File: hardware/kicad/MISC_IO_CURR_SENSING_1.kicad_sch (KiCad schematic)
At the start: 20 parts

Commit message: starting erc check
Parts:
- C39: footprint Capacitor_SMD:C_0603_1608Metric -> 5v rail sm-easyedapro:C0603
- C40: footprint Capacitor_SMD:C_0805_2012Metric -> 5v rail sm-easyedapro:C0805
- C41, C42, C43: footprint Capacitor_SMD:C_0201_0603Metric -> 5v rail sm-easyedapro:C0201
- CUR_1: footprint Package_DFN_QFN:QFN-16-1EP_4x4mm_P0.65mm_EP2.2x2.2mm -> 5v rail sm-easyedapro:QFN-16_L4.0-W4.0-P0.65-TL-EP2.2
- R100, R101, R102, R96, R97, R99: footprint Resistor_SMD:R_0402_1005Metric -> 5v rail sm-easyedapro:R0402; LCSC Part Name 10Ω ±1% 50mW 厚膜电阻 -> 厚膜电阻 10Ω ±1% 62.5mW; Manufacturer UNI-ROYAL(厚声) -> YAGEO(国巨); Manufacturer Part 0201WMF100JTEE -> RC0402FR-0710RL; Supplier Part C270817 -> C138066
- R98: footprint Resistor_SMD:R_0402_1005Metric -> 5v rail sm-easyedapro:R0402; LCSC Part Name 厚膜电阻 10kΩ ±1% 50mW -> 10kΩ ±1% 62.5mW 厚膜电阻; Manufacturer YAGEO(国巨) -> UNI-ROYAL(厚声); Manufacturer Part RC0201FR-0710KL -> 0402WGF1002TCE; Supplier Part C106225 -> C25744

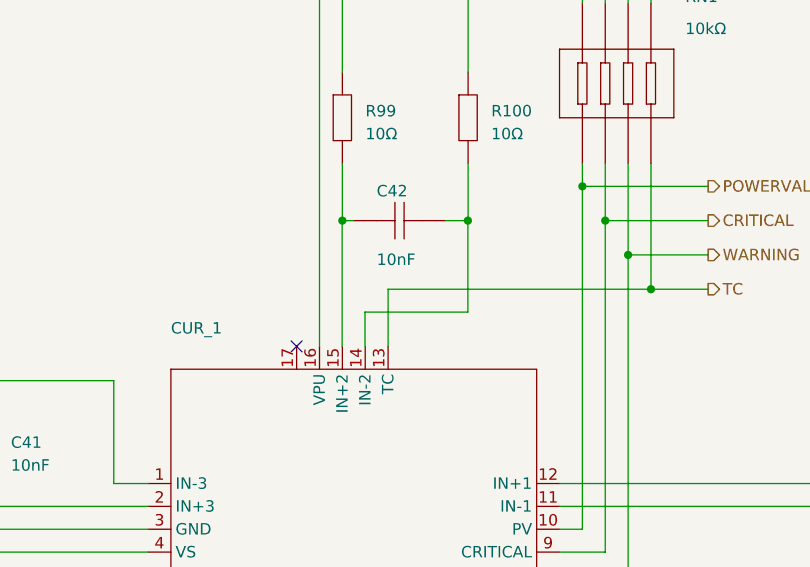
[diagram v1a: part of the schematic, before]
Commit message: current sensor done for breakout ports
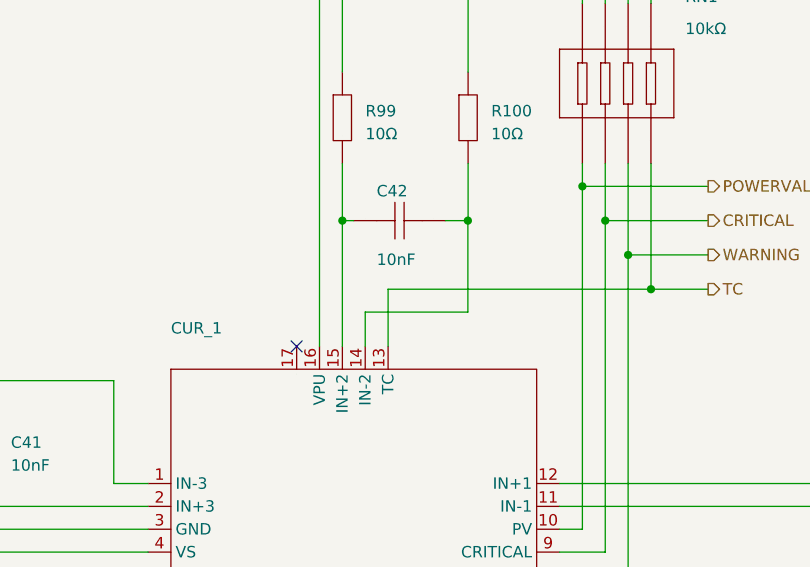
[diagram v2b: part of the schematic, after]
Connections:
- net at CUR_1.14 (IN-2): now also C42.2, R100.2
- net at CUR_1.15 (IN+2): now also C42.1, R99.2
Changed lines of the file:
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@@
 	(wire
 		(pts
-			(xy 154.9146 80.01) (xy 154.9146 93.98)
+			(xy 154.94 80.01) (xy 154.94 93.98)
 		)
 		(stroke
@@
 	(wire
 		(pts
-			(xy 157.4546 93.98) (xy 157.4546 90.17)
+			(xy 157.48 93.98) (xy 157.48 90.17)
 		)
 		(stroke
@@
 	(wire
 		(pts
-			(xy 154.94 80.01) (xy 154.9146 80.01)
-		)
-		(stroke
-			(width 0)
-			(type default)
-		)
-	)
-	(wire
-		(pts
 			(xy 181.61 73.66) (xy 181.61 76.2)
 		)
@@
 	(wire
 		(pts
-			(xy 168.8846 90.17) (xy 157.4546 90.17)
-		)
-		(stroke
+			(xy 168.8846 90.17) (xy 157.48 90.17)
+		)
+		(stroke

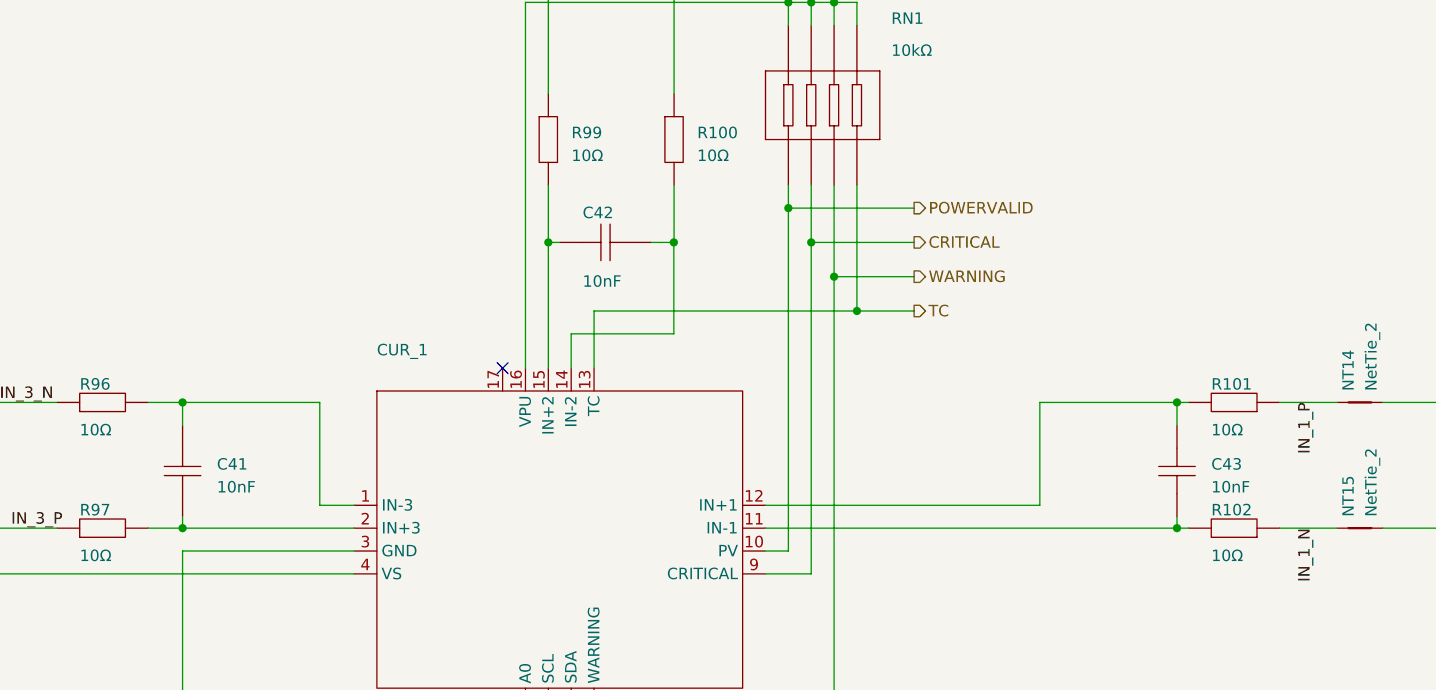
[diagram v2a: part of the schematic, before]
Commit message: flipped spots for 12v ports
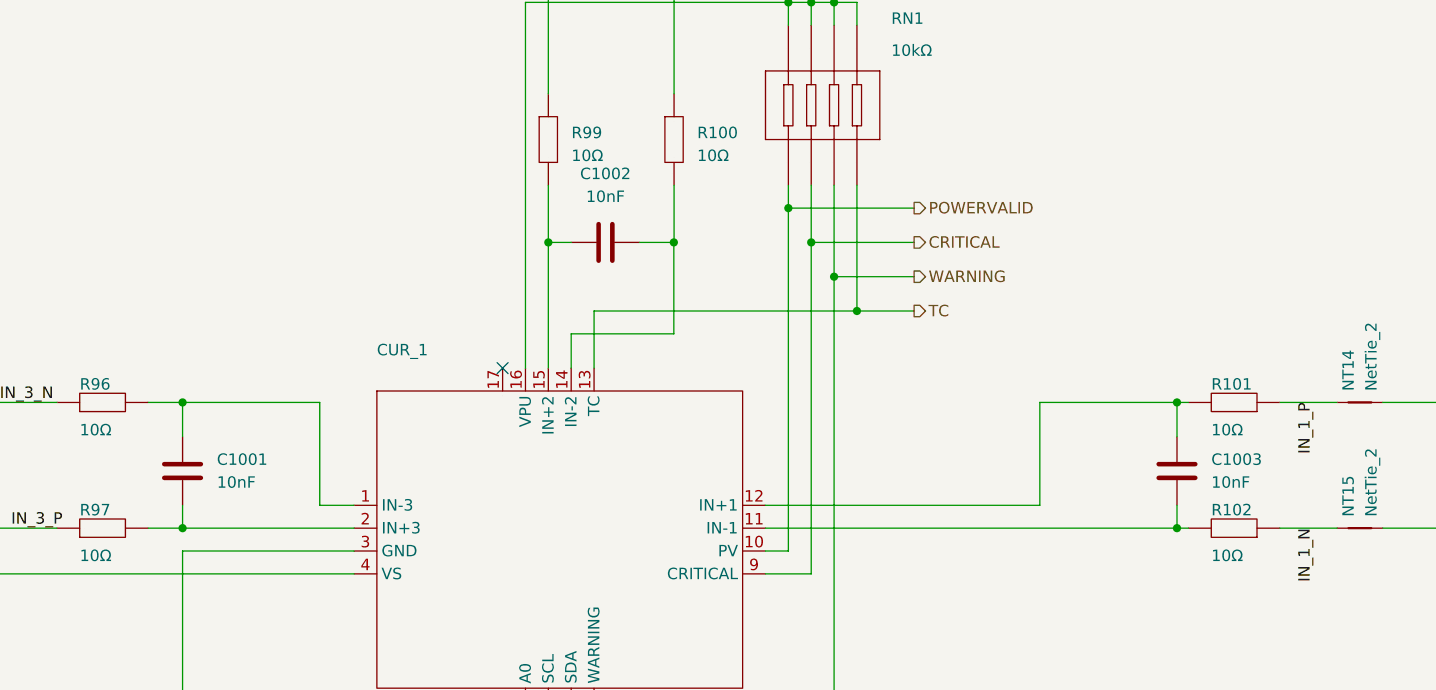
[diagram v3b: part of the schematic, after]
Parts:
- removed C41, C42, C43: 10nF, 5v rail sm-easyedapro:C0201, symbol 5v rail sm-easyedapro:TCC0201X7R103K500ZT
- added C1001, C1002, C1003: 10nF, Capacitor_SMD:C_0402_1005Metric, symbol Device:C
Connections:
- net at CUR_1.1 (IN-3), R96.2: now also C1001.1
- net at CUR_1.11 (IN-1), R102.2: now also C1003.1
- net at CUR_1.12 (IN+1), R101.2: now also C1003.2
- net at CUR_1.14 (IN-2), R100.2: now also C1002.2
- net at CUR_1.15 (IN+2), R99.2: now also C1002.1
- net at CUR_1.2 (IN+3), R97.2: now also C1001.2

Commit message: updating symbols to use kicad footprints where possible
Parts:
- C39: footprint 5v rail sm-easyedapro:C0603 -> Capacitor_SMD:C_0603_1608Metric
- C40: footprint 5v rail sm-easyedapro:C0805 -> Capacitor_SMD:C_0805_2012Metric
- R100, R101, R102, R96, R97, R98, R99: footprint 5v rail sm-easyedapro:R0402 -> Resistor_SMD:R_0402_1005Metric
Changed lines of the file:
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@@
 			)
 		)
-		(property "Footprint" "5v rail sm-easyedapro:R0402"
+		(property "Footprint" "Resistor_SMD:R_0402_1005Metric"
 			(at 231.14 111.76 0)
 			(effects
@@
 			)
 		)
-		(property "Footprint" "5v rail sm-easyedapro:R0402"
+		(property "Footprint" "Resistor_SMD:R_0402_1005Metric"
 			(at 142.24 138.43 0)
 			(effects
@@
 			)
 		)
-		(property "Footprint" "5v rail sm-easyedapro:R0402"
+		(property "Footprint" "Resistor_SMD:R_0402_1005Metric"
 			(at 168.91 68.58 0)
 			(effects
@@
 			)
 		)
-		(property "Footprint" "5v rail sm-easyedapro:C0805"
+		(property "Footprint" "Capacitor_SMD:C_0805_2012Metric"
 			(at 63.5 127 0)
 			(effects
@@
 			)
 		)
-		(property "Footprint" "5v rail sm-easyedapro:R0402"
+		(property "Footprint" "Resistor_SMD:R_0402_1005Metric"
 			(at 105.41 111.76 0)
 			(effects
@@
 			)
 		)
-		(property "Footprint" "5v rail sm-easyedapro:R0402"
+		(property "Footprint" "Resistor_SMD:R_0402_1005Metric"
 			(at 154.94 68.58 0)
 			(effects
@@
 			)
 		)
-		(property "Footprint" "5v rail sm-easyedapro:C0603"
+		(property "Footprint" "Capacitor_SMD:C_0603_1608Metric"
 			(at 46.99 127 0)
 			(effects
@@
 			)
 		)
-		(property "Footprint" "5v rail sm-easyedapro:R0402"
+		(property "Footprint" "Resistor_SMD:R_0402_1005Metric"
 			(at 231.14 97.79 0)
 			(effects
@@
 			)
 		)
-		(property "Footprint" "5v rail sm-easyedapro:R0402"
+		(property "Footprint" "Resistor_SMD:R_0402_1005Metric"
 			(at 105.41 97.79 0)
 			(effects

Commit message: switched some more
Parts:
- CUR_1: footprint 5v rail sm-easyedapro:QFN-16_L4.0-W4.0-P0.65-TL-EP2.2 -> Package_DFN_QFN:QFN-16-1EP_4x4mm_P0.65mm_EP2.2x2.2mm
- RN1: footprint 5v rail sm-easyedapro:RES-ARRAY-SMD_0603-8P-L3.2-W1.6-BL -> Resistor_SMD:R_Array_Convex_4x0603
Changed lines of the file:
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@@
 			)
 		)
-		(property "Footprint" "5v rail sm-easyedapro:QFN-16_L4.0-W4.0-P0.65-TL-EP2.2"
+		(property "Footprint" "Package_DFN_QFN:QFN-16-1EP_4x4mm_P0.65mm_EP2.2x2.2mm"
 			(at 156.21 113.03 0)
 			(effects
@@
 			)
 		)
-		(property "Footprint" "5v rail sm-easyedapro:RES-ARRAY-SMD_0603-8P-L3.2-W1.6-BL"
+		(property "Footprint" "Resistor_SMD:R_Array_Convex_4x0603"
 			(at 185.42 64.77 0)
 			(effects

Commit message: various erc fixes
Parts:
- CUR_1: footprint Package_DFN_QFN:QFN-16-1EP_4x4mm_P0.65mm_EP2.2x2.2mm -> Package_DFN_QFN:Texas_RGV0016A_VQFN-16-1EP_4x4mm_P0.65mm_EP2.1x2.1mm
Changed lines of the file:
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@@
 			)
 		)
-		(property "Footprint" "Package_DFN_QFN:QFN-16-1EP_4x4mm_P0.65mm_EP2.2x2.2mm"
+		(property "Footprint" "Package_DFN_QFN:Texas_RGV0016A_VQFN-16-1EP_4x4mm_P0.65mm_EP2.1x2.1mm"
 			(at 156.21 113.03 0)
 			(effects

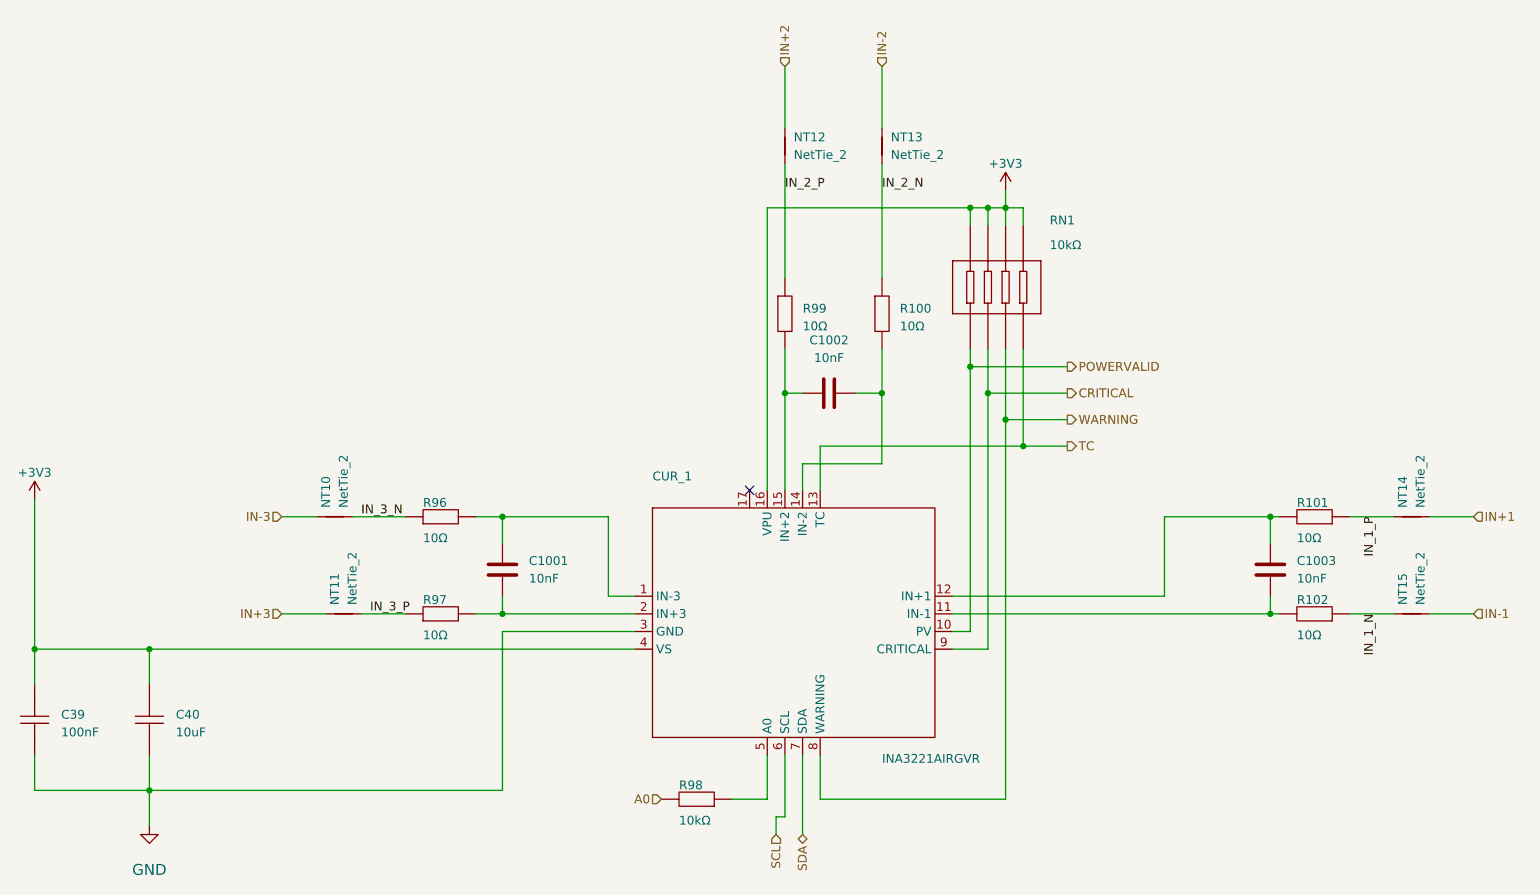
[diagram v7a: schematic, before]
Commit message: fixing inconsistencies in value convention
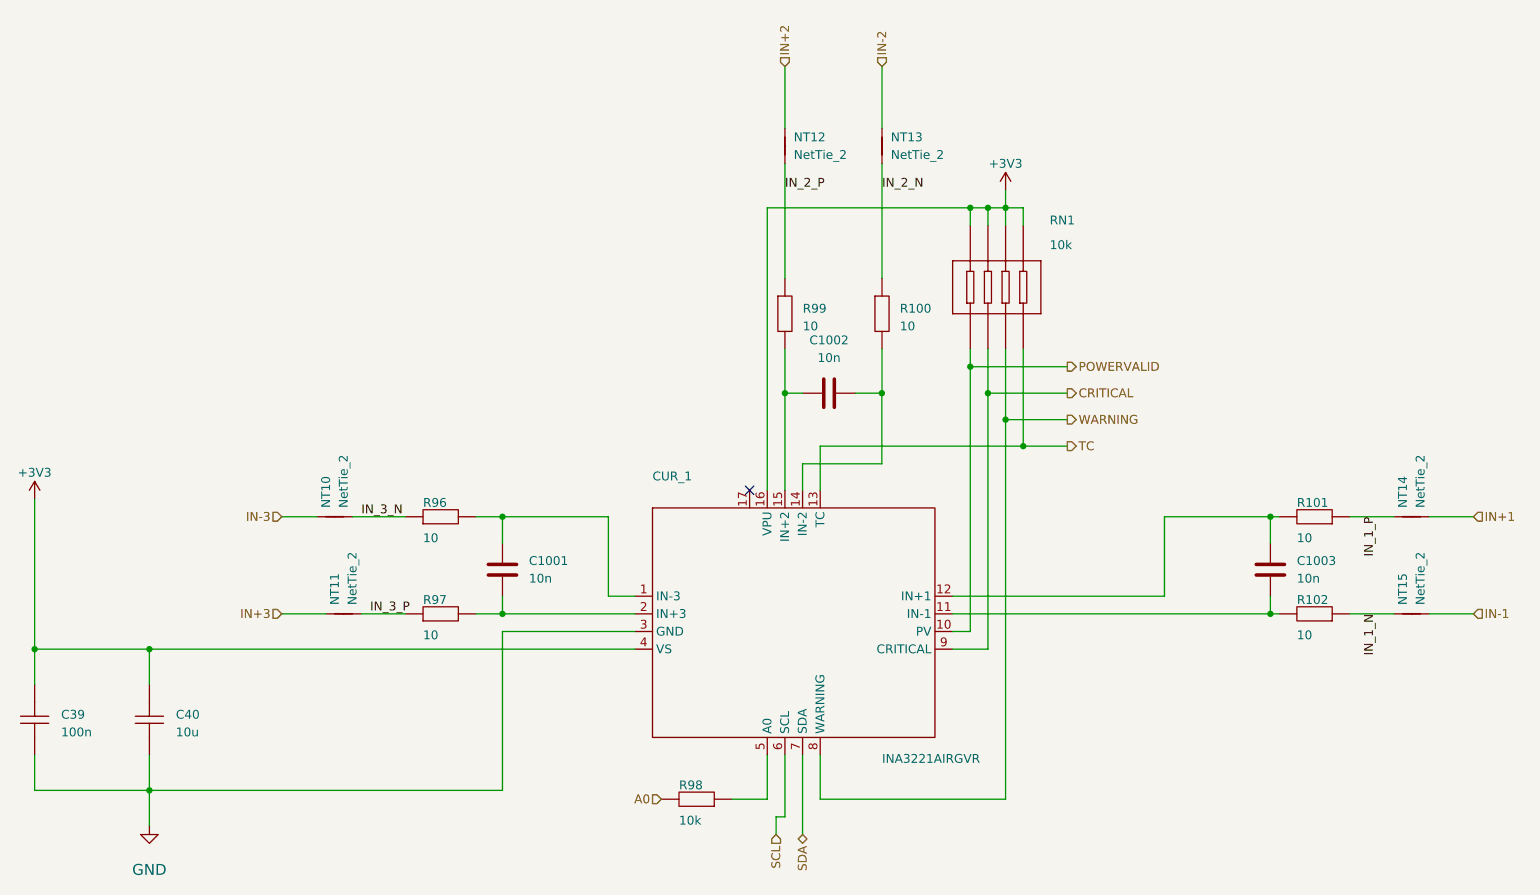
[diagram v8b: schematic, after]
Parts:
- C1001, C1002, C1003: value 10nF -> 10n
- C39: value 100nF -> 100n
- C40: value 10uF -> 10u
- R100, R101, R102, R96, R97, R99: value 10Ω -> 10
- R98, RN1: value 10kΩ -> 10k
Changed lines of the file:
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@@
 			)
 		)
-		(property "Value" "10nF"
+		(property "Value" "10n"
 			(at 228.6 106.6799 0)
 			(effects
@@
 			)
 		)
-		(property "Value" "10Ω"
+		(property "Value" "10"
 			(at 228.6 115.57 0)
 			(effects
@@
 			)
 		)
-		(property "Value" "10kΩ"
+		(property "Value" "10k"
 			(at 139.7 142.24 0)
 			(effects
@@
 			)
 		)
-		(property "Value" "10Ω"
+		(property "Value" "10"
 			(at 171.4754 71.12 90)
 			(effects
@@
 			)
 		)
-		(property "Value" "10uF"
+		(property "Value" "10u"
 			(at 67.31 129.54 90)
 			(effects
@@
 			)
 		)
-		(property "Value" "10nF"
+		(property "Value" "10n"
 			(at 161.29 74.93 90)
 			(effects
@@
 			)
 		)
-		(property "Value" "10Ω"
+		(property "Value" "10"
 			(at 102.87 115.57 0)
 			(effects
@@
 			)
 		)
-		(property "Value" "10Ω"
+		(property "Value" "10"
 			(at 157.5054 71.12 90)
 			(effects
@@
 			)
 		)
-		(property "Value" "10nF"
+		(property "Value" "10n"
 			(at 118.11 106.6799 0)
 			(effects
@@
 			)
 		)
-		(property "Value" "100nF"
+		(property "Value" "100n"
 			(at 50.8 129.54 90)
 			(effects
@@
 			)
 		)
-		(property "Value" "10Ω"
+		(property "Value" "10"
 			(at 228.6 101.6 0)
 			(effects
@@
 			)
 		)
-		(property "Value" "10kΩ"
+		(property "Value" "10k"
 			(at 193.04 59.436 0)
 			(effects
@@
 			)
 		)
-		(property "Value" "10Ω"
+		(property "Value" "10"
 			(at 102.87 101.6 0)
 			(effects
